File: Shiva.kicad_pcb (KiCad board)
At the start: 2 copper layers, 99.8 x 99.8 mm, 72 parts, among them J1 JACK_FEMALE_STEREO, J2 JACK_FEMALE_STEREO, J3 JACK_FEMALE_STEREO, J4 JACK_FEMALE_STEREO, J5 JACK_FEMALE_STEREO, J6 JACK_FEMALE_STEREO, J7 JACK_FEMALE_STEREO, J8 JACK_FEMALE_STEREO, P1 DIN_5, U1 LTC6242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

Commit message: Add logos, copper front plane
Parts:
- added REF**: Symbol_OSHW-Logo_SilkScreen, Symbols:Symbol_OSHW-Logo_SilkScreen, F.Cu at (185.9, 59.7)
- moved G*** 76.0 mm to (143.5, 146.3)
- moved G*** 75.3 mm to (144.8, 128.3)
- moved D11 74.0 mm to (187.5, 96.5)
- moved D13 74.0 mm to (187.5, 118.4)
- moved D9 74.0 mm to (187.5, 140.5)
- moved J5 74.0 mm to (182.9, 136.1)
- moved J6 74.0 mm to (182.9, 93.0)
- moved J7 74.0 mm to (182.9, 114.6)
- moved J8 74.0 mm to (182.9, 70.7)
- moved R13 74.0 mm to (183.5, 136.1)
- moved R14 74.0 mm to (183.5, 92.3)
- moved R15 74.0 mm to (183.5, 113.9)
- moved R16 74.0 mm to (183.6, 70.9)
- moved R21 74.0 mm to (187.3, 136.1)
- moved R22 74.0 mm to (187.3, 92.3)
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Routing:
- added copper zone on F.Cu, net VCC
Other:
- board text added: "CHANNEL 1"
- board text added: "CHANNEL 2"
- board text added: "CHANNEL 3"
- board text added: "CHANNEL 4"
- board text added: "CHANNEL 5"
- board text added: "CHANNEL 6"
- board text added: "CHANNEL 7"
- board text added: "CHANNEL 8"
- board text added: "David Estevez Fernandez"
- board text added: "MIDI OUT"
- board text added: "Shiva 0.1"
- board text added: "TEENSY 3.x"

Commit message: Add drills and heatsinking
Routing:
- net Net-(C4-Pad1): track 28.5 -> 17.4 mm
- net GND: track 200.6 -> 192.0 mm, vias 2 -> 3
- net VCC: track 386.5 -> 389.7 mm
- added copper zone on F.Cu, net Net-(C4-Pad1)
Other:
- board text removed: "(thermal gnd plane here)"
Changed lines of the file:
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@@
     (area 94.309999 52.653999 194.310001 152.654001)
     (thickness 1.6)
-    (drawings 22)
-    (tracks 1063)
+    (drawings 21)
+    (tracks 1057)
     (zones 0)
     (modules 73)
@@
     (effects (font (size 3 2) (thickness 0.5)) (justify mirror))
   )
-  (gr_text "(thermal gnd plane here)" (at 124.206 49.784) (layer Cmts.User)
-    (effects (font (size 1.5 1.5) (thickness 0.3)))
-  )
   (gr_line (start 191.135 73.279) (end 191.135 141.859) (angle 90) (layer Dwgs.User) (width 0.2))
   (gr_line (start 99.41 52.754) (end 189.21 52.754) (angle 90) (layer Edge.Cuts) (width 0.2))
@@
   (gr_arc (start 99.41 147.554) (end 99.41 152.554) (angle 90) (layer Edge.Cuts) (width 0.2))
   (gr_arc (start 99.41 57.754) (end 94.41 57.754) (angle 90) (layer Edge.Cuts) (width 0.2))
+  (segment (start 120.396 63.754) (end 123.305 63.754) (width 0.25) (layer F.Cu) (net 1))
+  (segment (start 120.015 63.373) (end 120.396 63.754) (width 0.25) (layer F.Cu) (net 1))
+  (via (at 120.396 63.754) (size 0.6) (drill 0.4) (layers F.Cu B.Cu) (net 1))
+  (segment (start 120.015 61.595) (end 120.015 63.373) (width 0.25) (layer F.Cu) (net 1))
+  (segment (start 123.305 63.754) (end 124.065 62.994) (width 0.25) (layer F.Cu) (net 1))
   (segment (start 162.179 94.107) (end 162.179 94.361) (width 0.25) (layer F.Cu) (net 1))
   (segment (start 162.56 94.742) (end 166.898 94.742) (width 0.25) (layer F.Cu) (net 1))
@@
   (segment (start 106.895 72.009) (end 104.855 72.009) (width 0.25) (layer F.Cu) (net 1))
   (segment (start 104.855 72.009) (end 104.775 72.089) (width 0.25) (layer F.Cu) (net 1))
-  (segment (start 124.065 62.994) (end 124.065 61.101) (width 0.25) (layer F.Cu) (net 1))
-  (segment (start 126.472 58.694) (end 131.445 58.694) (width 0.25) (layer F.Cu) (net 1))
-  (segment (start 124.065 61.101) (end 126.472 58.694) (width 0.25) (layer F.Cu) (net 1))
-  (segment (start 120.015 61.595) (end 121.031 61.595) (width 0.25) (layer F.Cu) (net 1))
-  (segment (start 121.031 61.595) (end 122.43 62.994) (width 0.25) (layer F.Cu) (net 1))
-  (segment (start 122.43 62.994) (end 124.065 62.994) (width 0.25) (layer F.Cu) (net 1))
   (segment (start 189.738 89.408) (end 189.738 90.852) (width 0.25) (layer F.Cu) (net 1))
   (segment (start 189.738 90.852) (end 189.865 90.979) (width 0.25) (layer F.Cu) (net 1))
@@
   (segment (start 128.665 62.994) (end 128.905 63.234) (width 0.25) (layer F.Cu) (net 27))
   (segment (start 128.905 63.234) (end 128.905 65.8368) (width 0.25) (layer F.Cu) (net 27))
+  (segment (start 132.08 55.118) (end 132.08 54.61) (width 0.25) (layer F.Cu) (net 28))
+  (segment (start 112.776 54.356) (end 112.776 60.452) (width 0.25) (layer F.Cu) (net 28))
+  (segment (start 113.284 53.848) (end 112.776 54.356) (width 0.25) (layer F.Cu) (net 28))
+  (segment (start 131.318 53.848) (end 113.284 53.848) (width 0.25) (layer F.Cu) (net 28))
+  (segment (start 132.08 54.61) (end 131.318 53.848) (width 0.25) (layer F.Cu) (net 28))
   (segment (start 192.024 119.38) (end 192.278 119.634) (width 0.25) (layer F.Cu) (net 28))
   (segment (start 192.278 119.634) (end 192.278 119.888) (width 0.25) (layer F.Cu) (net 28))
@@
   (segment (start 192.024 76.239) (end 192.278 76.239) (width 0.25) (layer F.Cu) (net 28))
   (segment (start 192.278 76.239) (end 192.278 76.2) (width 0.25) (layer F.Cu) (net 28))
-  (segment (start 116.84 64.008) (end 116.84 56.642) (width 0.25) (layer F.Cu) (net 28))
-  (segment (start 116.84 56.642) (end 118.364 55.118) (width 0.25) (layer F.Cu) (net 28))
-  (segment (start 118.364 55.118) (end 137.922 55.118) (width 0.25) (layer F.Cu) (net 28))
+  (segment (start 132.08 55.118) (end 137.922 55.118) (width 0.25) (layer F.Cu) (net 28))
   (segment (start 137.922 55.118) (end 140.208 57.404) (width 0.25) (layer F.Cu) (net 28))
   (segment (start 140.208 57.404) (end 188.468 57.404) (width 0.25) (layer F.Cu) (net 28))
@@
   (segment (start 118.11 65.278) (end 116.84 64.008) (width 0.25) (layer F.Cu) (net 28))
   (segment (start 116.84 64.008) (end 113.284 60.452) (width 0.25) (layer F.Cu) (net 28))
-  (segment (start 113.284 60.452) (end 97.79 60.452) (width 0.25) (layer F.Cu) (net 28))
-  (segment (start 97.79 60.452) (end 96.012 62.23) (width 0.25) (layer F.Cu) (net 28))
+  (segment (start 113.284 60.452) (end 112.776 60.452) (width 0.25) (layer F.Cu) (net 28))
+  (segment (start 112.776 60.452) (end 97.79 60.452) (width 0.25) (layer F.Cu) (net 28))
   (segment (start 96.012 62.23) (end 96.012 65.024) (width 0.25) (layer F.Cu) (net 28))
+  (segment (start 97.79 60.452) (end 96.012 62.23) (width 0.25) (layer F.Cu) (net 28))
   (segment (start 96.012 65.024) (end 96.012 65.278) (width 0.25) (layer F.Cu) (net 28))
   (segment (start 96.012 65.278) (end 96.012 65.532) (width 0.25) (layer F.Cu) (net 28))
@@
   (segment (start 151.05 67.959) (end 156.845 73.754) (width 0.25) (layer F.Cu) (net 70))
   (segment (start 156.845 73.754) (end 156.845 76.374) (width 0.25) (layer F.Cu) (net 70))
-  (segment (start 126.365 65.024) (end 126.111 64.77) (width 0.25) (layer F.Cu) (net 71))
-  (segment (start 126.111 64.77) (end 125.984 64.77) (width 0.25) (layer F.Cu) (net 71))
-  (segment (start 126.365 64.516) (end 126.111 64.77) (width 0.25) (layer F.Cu) (net 71))
-  (segment (start 125.984 64.77) (end 126.238 64.77) (width 0.25) (layer F.Cu) (net 71))
-  (segment (start 126.111 64.77) (end 126.238 64.77) (width 0.25) (layer F.Cu) (net 71))
-  (segment (start 118.491 58.293) (end 117.856 58.928) (width 0.25) (layer F.Cu) (net 71))
-  (segment (start 117.856 58.928) (end 117.856 64.008) (width 0.25) (layer F.Cu) (net 71))
-  (segment (start 117.856 64.008) (end 118.618 64.77) (width 0.25) (layer F.Cu) (net 71))
-  (segment (start 118.618 64.77) (end 125.984 64.77) (width 0.25) (layer F.Cu) (net 71))
-  (segment (start 118.491 58.293) (end 120.015 58.293) (width 0.25) (layer F.Cu) (net 71))
+  (segment (start 126.365 56.894) (end 126.365 62.994) (width 0.25) (layer F.Cu) (net 71))
   (segment (start 126.365 62.994) (end 126.365 64.516) (width 0.25) (layer F.Cu) (net 71))
   (segment (start 126.365 64.516) (end 126.365 65.024) (width 0.25) (layer F.Cu) (net 71))
@@
     (connect_pads (clearance 0.508))
     (min_thickness 0.254)
-    (fill yes (arc_segments 16) (thermal_gap 0.508) (thermal_bridge_width 0.508))
+    (fill yes (arc_segments 16) (thermal_gap 0.508) (thermal_bridge_width 0.508) (smoothing chamfer))
     (polygon
       (pts
@@
       )
     )
+    (polygon
+      (pts        (xy 113.538 54.356) (xy 113.538 59.436) (xy 118.618 64.77) (xy 125.476 64.77) (xy 126.492 62.992)
+        (xy 131.318 62.992) (xy 131.318 54.356) (xy 113.538 54.356)
+      )
+    )
+  )
+  (zone (net 71) (net_name "Net-(C4-Pad1)") (layer F.Cu) (hatch edge 0.508)
+    (connect_pads (clearance 0.508))
+    (min_thickness 0.254)
+    (fill yes (arc_segments 16) (thermal_gap 0.508) (thermal_bridge_width 0.508) (smoothing chamfer))
+    (polygon
+      (pts
+        (xy 130.556 62.484) (xy 125.73 62.484) (xy 124.968 64.262) (xy 118.872 64.262) (xy 114.046 59.182)
+        (xy 114.046 54.864) (xy 130.81 54.864) (xy 130.556 62.484)
+      )
+    )
+  )
+  (zone (net 0) (net_name "") (layer F.Mask) (hatch edge 0.508)
+    (connect_pads (clearance 0.508))
+    (min_thickness 0.254)
+    (fill yes (arc_segments 16) (thermal_gap 0.508) (thermal_bridge_width 0.508) (smoothing chamfer))
+    (polygon
+      (pts
+        (xy 130.048 61.468) (xy 122.174 61.468) (xy 121.412 59.944) (xy 118.11 59.944) (xy 118.11 61.722)
+        (xy 116.586 61.722) (xy 114.046 59.182) (xy 114.046 54.864) (xy 130.048 54.864) (xy 130.048 61.214)
+      )
+    )

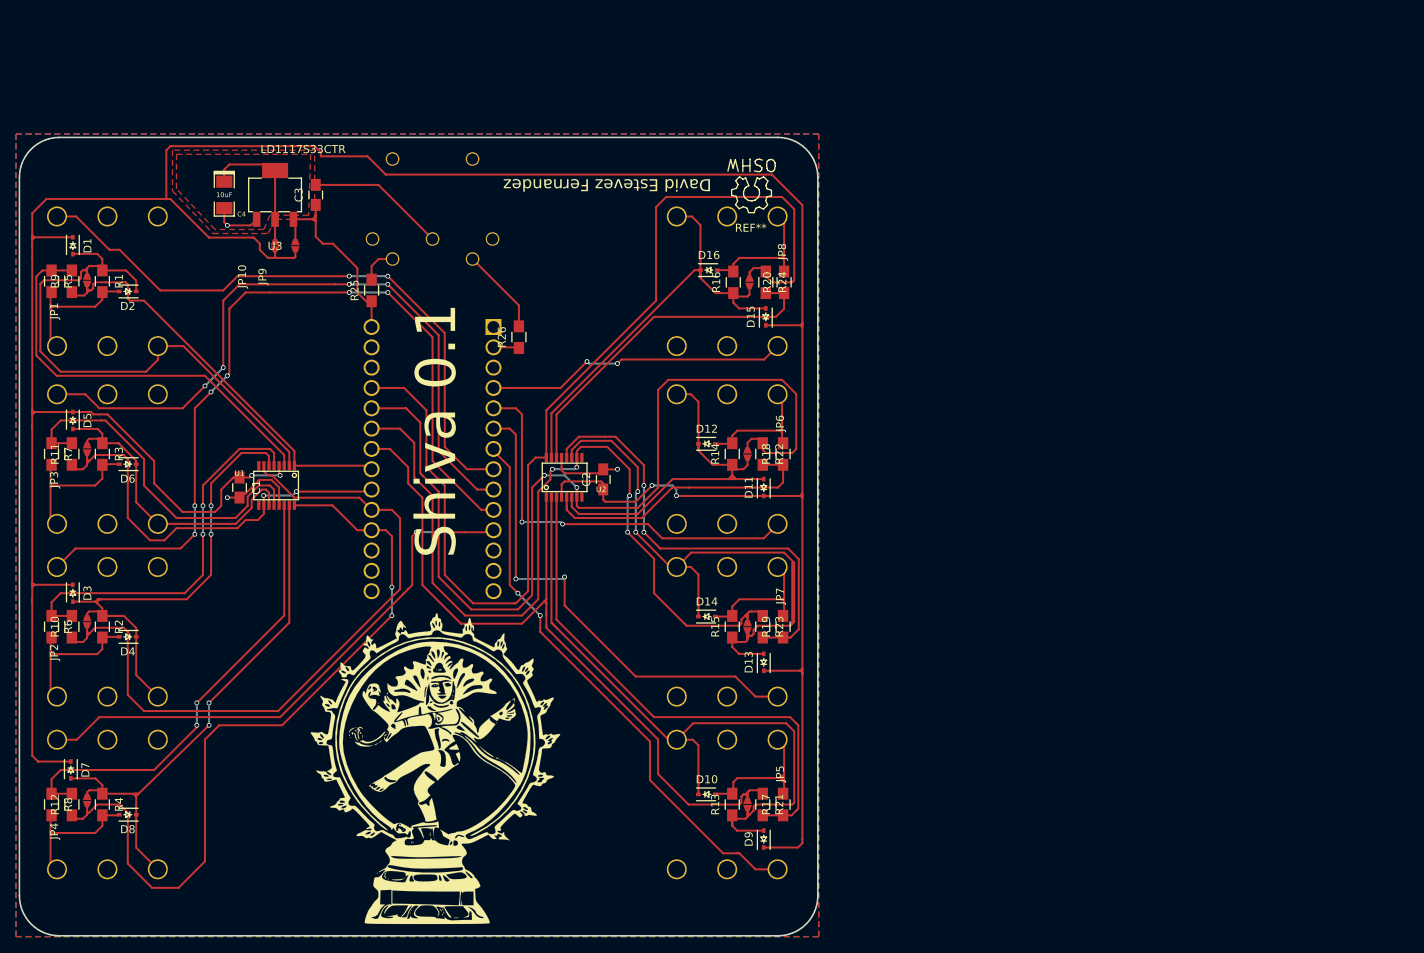
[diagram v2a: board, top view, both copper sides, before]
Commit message: Fix bug with midi tx. Finish silkscreen
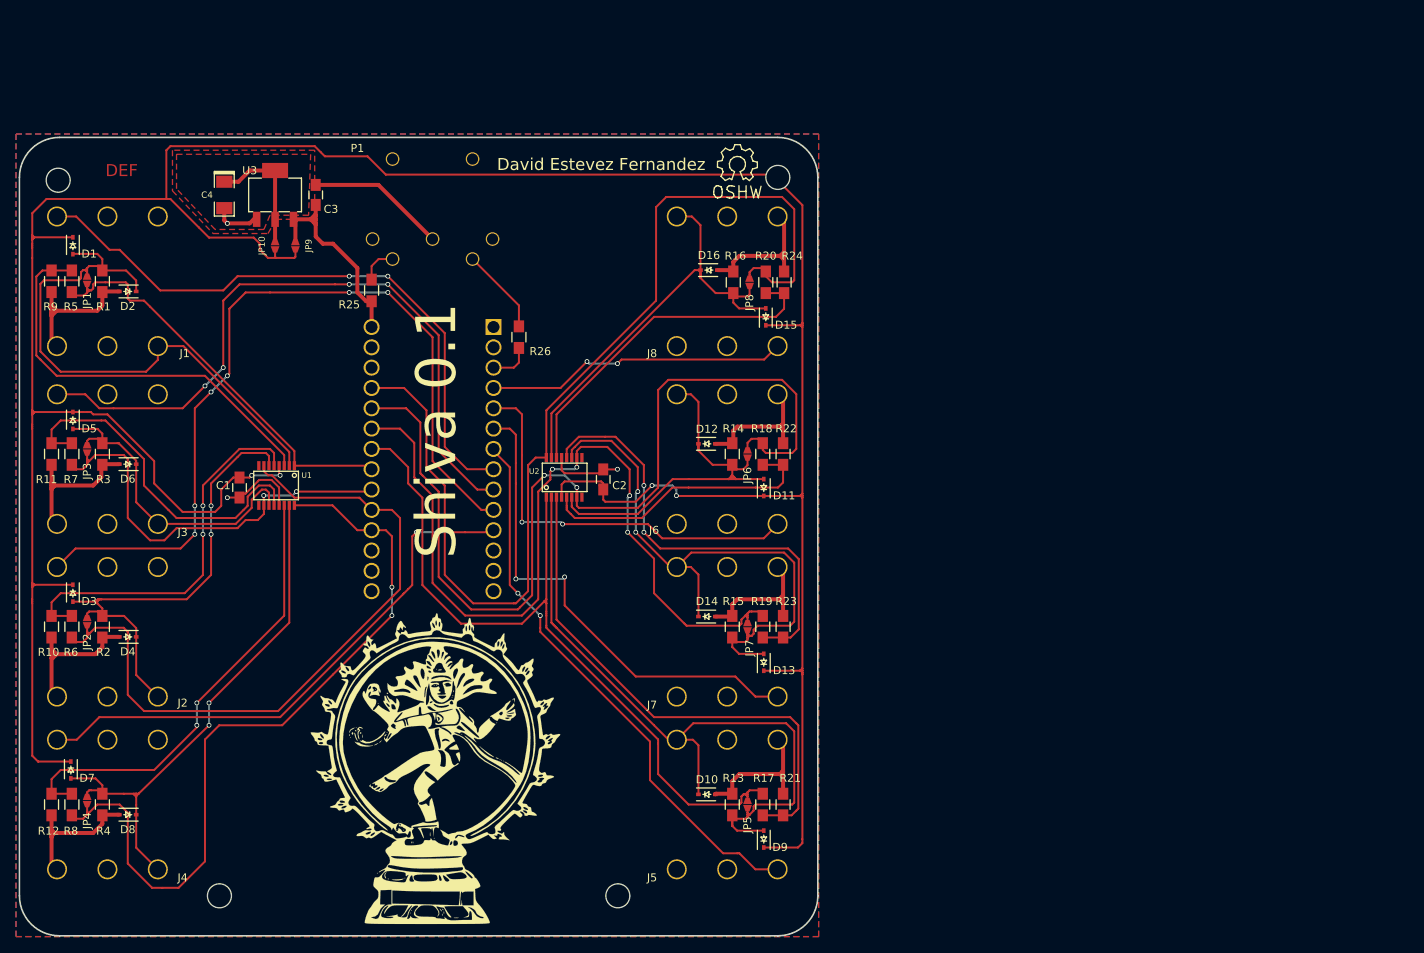
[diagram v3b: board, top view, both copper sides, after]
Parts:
- added Mechanical_drill_3mm: , def-footprints:Mechanical_Drill_3mm, F.Cu at (99.4, 57.8)
- added Mechanical_drill_3mm: , def-footprints:Mechanical_Drill_3mm, F.Cu at (189.2, 57.8)
- added Mechanical_drill_3mm: , def-footprints:Mechanical_Drill_3mm, F.Cu at (119.4, 147.6)
- added Mechanical_drill_3mm: , def-footprints:Mechanical_Drill_3mm, F.Cu at (169.2, 147.6)
- moved REF** 3.98 mm to (184.2, 56.1), turned to 0 degrees
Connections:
- BOARD1 pad 2: /RX -> Net-(BOARD1-Pad2)
- BOARD1 pad 3: Net-(BOARD1-Pad3) -> /TX
- R26 pad 1: /RX -> /TX
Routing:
- net GND: track 192.0 -> 205.4 mm
- net +5V: track 26.1 -> 39.1 mm
- net Net-(D13-Pad2): track 83.5 -> 75.5 mm
- net /TX: track 0.00 -> 5.38 mm
- net /RX: track 3.21 -> 0.00 mm
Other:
- net class power added: clearance 0.2, trace_width 0.5, via_dia 0.6, via_drill 0.4
- board text added: "DEF"

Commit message: Modify silkscreen
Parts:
- removed REF**: Symbol_OSHW-Logo_SilkScreen, Symbols:Symbol_OSHW-Logo_SilkScreen
- added G***: OSHW-logo, def-footprints:Logo_OSHW_small, F.Cu at (128.5, 80.5)
- added G***: LOGO, def-footprints:Logo_OSHW_3x3cm, F.Cu at (145.5, 52.6)

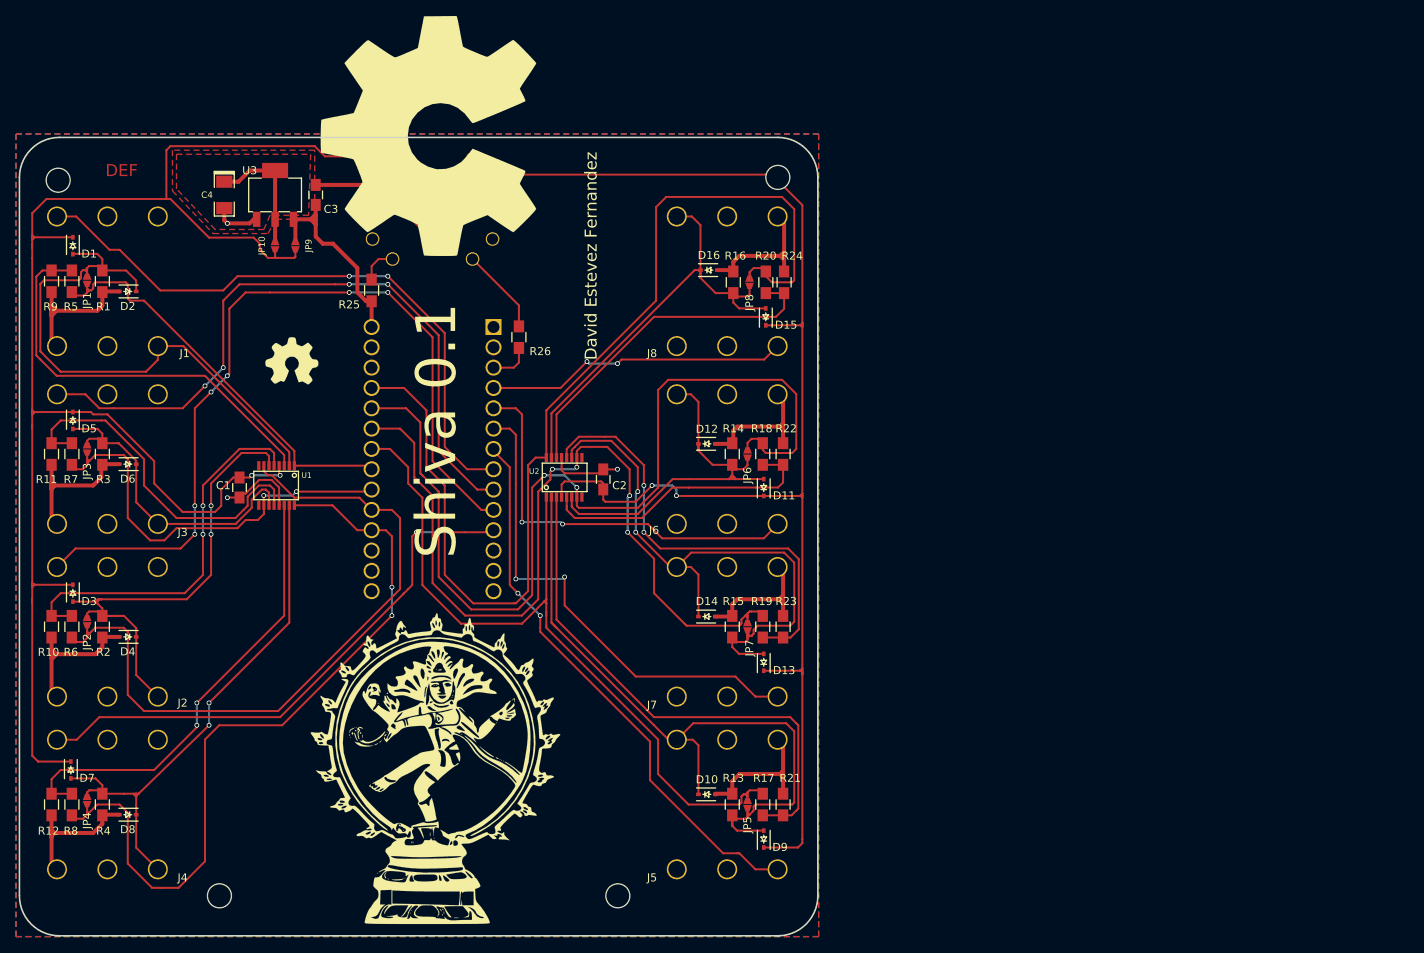
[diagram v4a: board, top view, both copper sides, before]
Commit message: Fixed solder jumpers
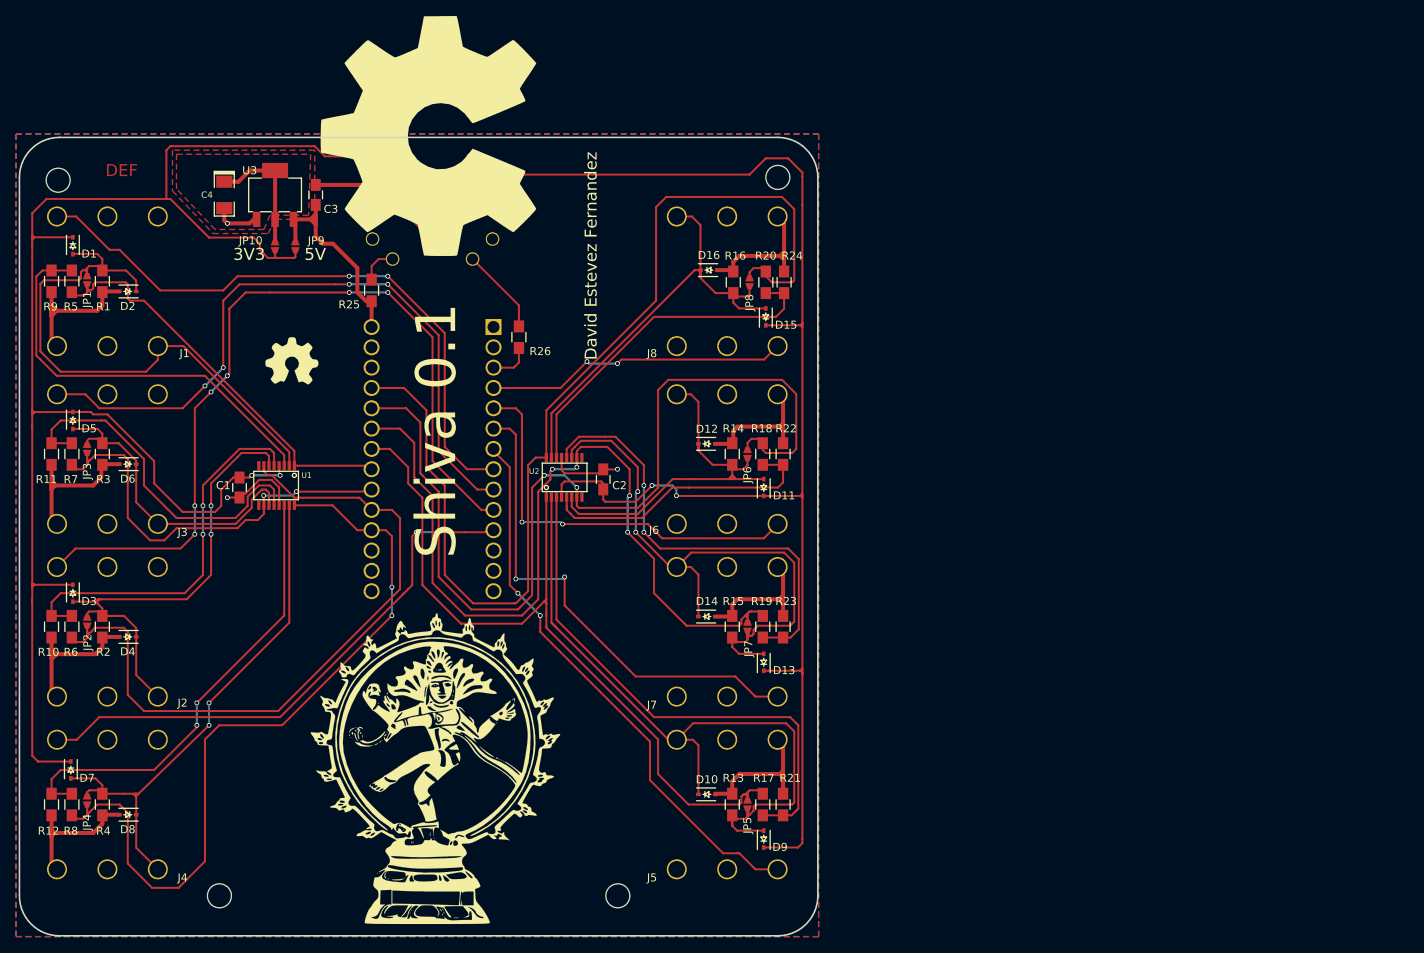
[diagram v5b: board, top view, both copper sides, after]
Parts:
- moved JP10 0.06 mm to (126.4, 66.4)
- moved JP9 0.06 mm to (128.9, 66.4)
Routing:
- net VCC: track 389.4 -> 393.5 mm
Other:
- board text added: "3V3"
- board text added: "5V"
